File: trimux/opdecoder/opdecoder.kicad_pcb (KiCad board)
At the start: 2 copper layers, 150 x 100 mm, 28 parts, among them J1 Conn_01x05, J11 Conn_01x05, J2 Conn_01x01, J3 Conn_01x01, J4 Conn_01x05, J5 Conn_01x01, J6 Conn_01x01, J7 Conn_01x01, J8 Conn_01x05, P1 CONN_01X03, P2 CONN_01X03, P3 CONN_01X03, U1 trimux, U10 trimux, U2 trimux, U3 trimux, U4 trimux, U5 trimux, U7 trimux, U8 trimux, U9 trimux

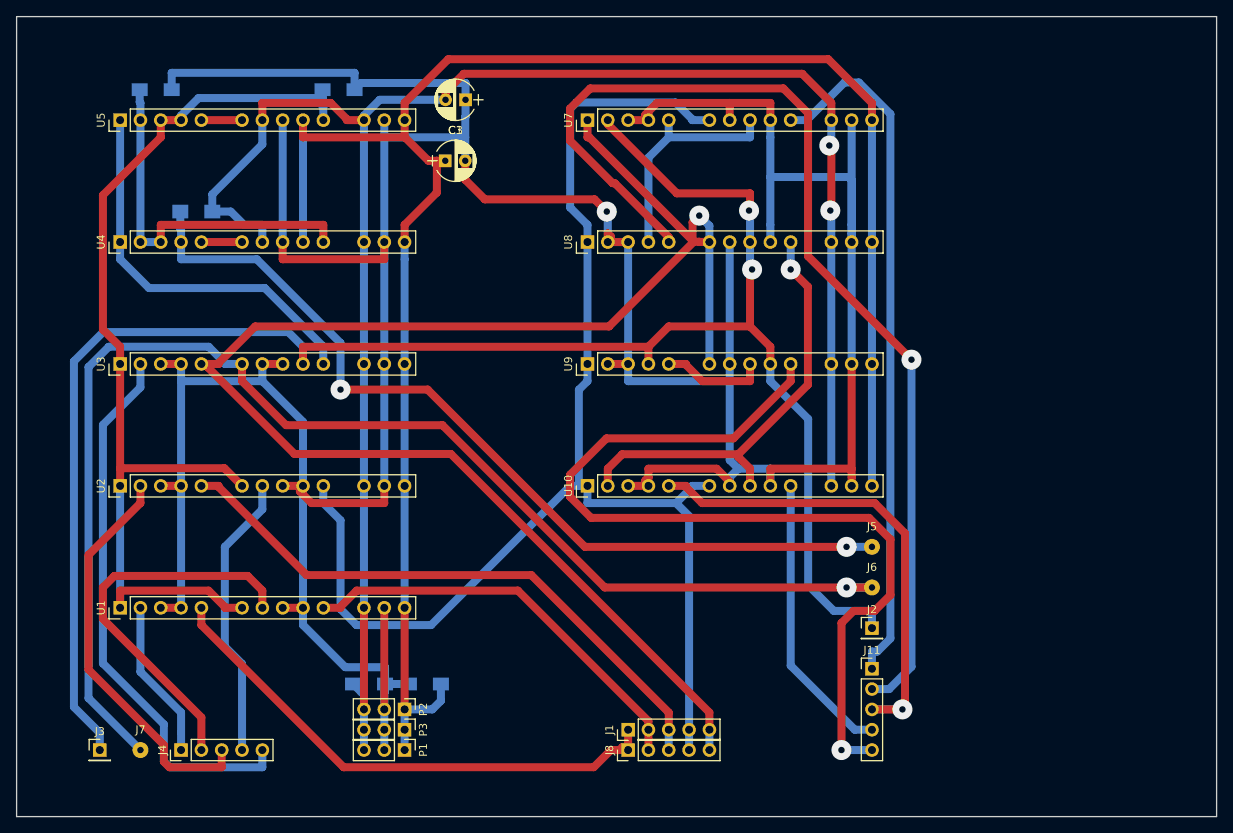
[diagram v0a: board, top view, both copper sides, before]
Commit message: opcode decoder
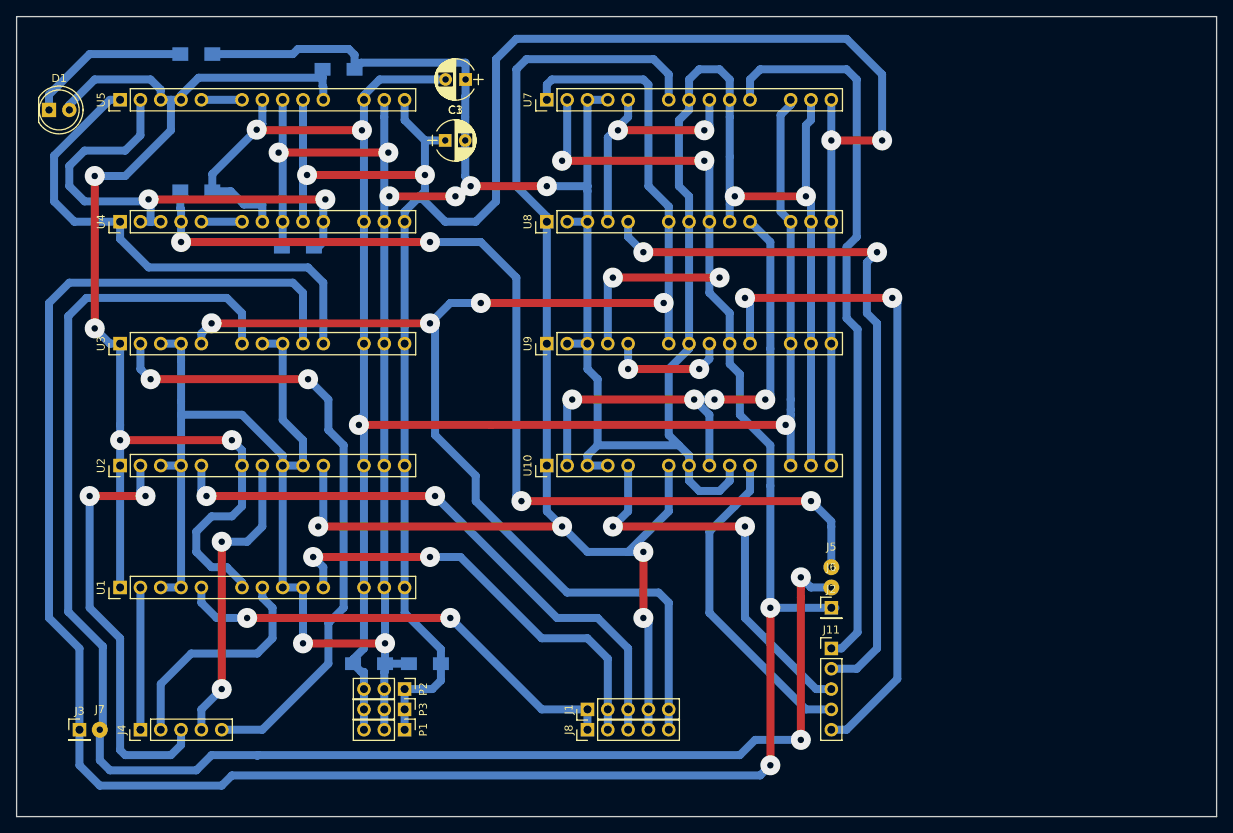
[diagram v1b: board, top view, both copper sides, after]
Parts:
- added D1: LED_bicolor, LEDs:LED_D5.0mm, F.Cu at (19.1, 26.7)
- added R2: 1k, Resistors_SMD:R_1206_HandSoldering, B.Cu at (37.5, 19.7)
- moved C5 26.5 mm to (50.2, 43.8), turned to 180 degrees
- moved J4 5.68 mm to (30.5, 104.1)
- moved J7 5.68 mm to (25.4, 104.1)
- moved J1 5.68 mm to (86.4, 101.6)
- moved J8 5.68 mm to (86.4, 104.1)
- moved U7 5.68 mm to (81.3, 25.4)
- moved U8 5.68 mm to (81.3, 40.6)
- moved U9 5.68 mm to (81.3, 55.9)
- moved J11 5.68 mm to (116.8, 94.0)
- moved J2 5.68 mm to (116.8, 88.9)
- moved J5 5.68 mm to (116.8, 83.8)
- moved U10 5.68 mm to (81.3, 71.1)
- moved J6 5.08 mm to (116.8, 86.4)
- moved J3 3.59 mm to (22.9, 104.1)
- moved P1 2.54 mm to (63.5, 104.1)
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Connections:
- net Net-(J5-Pad1) renamed /SKIP_SIGNAL
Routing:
- net /COUNTER_CLOCK: track 230.1 -> 323.4 mm, vias 2 -> 6
- net /SKIP_CLOCK: track 134.7 -> 91.2 mm, vias 1 -> 2
- net /INSTRUCTION_CYCLE: track 166.5 -> 199.3 mm, vias 1 -> 2
- net /MEMWRITE_CLOCK: track 113.8 -> 83.2 mm, vias 1 -> 2
- net +5V: track 233.9 -> 261.2 mm, vias 0 -> 4
- net /SKIP_NEXT_OP: track 124.9 -> 150.2 mm, vias 0 -> 4
- net Net-(D1-Pad1): track 0.00 -> 20.4 mm
- net /OPCODE_B4_SKIP_1: track 48.9 -> 28.9 mm
- net /OPCODE_4: track 199.0 -> 180.3 mm, vias 1 -> 4
- net Net-(C5-Pad1): track 46.2 -> 62.8 mm, vias 0 -> 2
- net Net-(U3-Pad11): track 49.5 -> 63.6 mm
- net /SKIP_SIGNAL: track 110.7 -> 123.8 mm, vias 2 -> 4
- net /OPA_CLOCK: track 62.0 -> 50.8 mm, vias 1 -> 2
- net Net-(U10-Pad2): track 54.8 -> 65.2 mm, vias 1 -> 4
- net /OPCODE_B4_SKIP_4: track 69.6 -> 79.6 mm, vias 0 -> 2
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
